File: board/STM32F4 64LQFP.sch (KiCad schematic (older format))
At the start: 15 parts, among them P2 SWD, U1 STM32F40X_LQFP64, X2 8MHz 10ppm

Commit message: - changed some more Vcc labels to +3V3 - combined all input connectors into one big connector - changed can transceiver to MAX3051 - removed HV pin from power connector -> divider now on PS board - updated components - startet layout
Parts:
- C10, C11, C12, C13, C14, C15, C16, C17, C31, C32, C35, C38: footprint CRF1:SMD-0603_c -> Capacitors_SMD:C_0805
- P2: footprint CRF1:MICRO_JST_6 -> Pin_Headers:Pin_Header_Straight_2x03
- U1: footprint CRF1:lqfp64_pad_mod -> Housings_QFP:LQFP-64_10x10mm_Pitch0.5mm
- X2: footprint CRF1:Crystal_5x3mm -> Crystals:Crystal_HC49-U_Vertical
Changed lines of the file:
@@
 F 0 "U1" H 5700 6200 60  0000 C CNN
 F 1 "STM32F40X_LQFP64" H 5750 1550 60  0000 C CNN
-F 2 "CRF1:lqfp64_pad_mod" H 5750 3900 60  0001 C CNN
+F 2 "Housings_QFP:LQFP-64_10x10mm_Pitch0.5mm" H 5750 3900 60  0001 C CNN
 F 3 "" H 5750 3900 60  0001 C CNN
 	1    5750 3900
@@
 F 0 "C17" H 7550 6450 50  0000 L CNN
 F 1 "2.2u" H 7550 6250 50  0000 L CNN
-F 2 "CRF1:SMD-0603_c" H 7500 6350 60  0001 C CNN
+F 2 "Capacitors_SMD:C_0805" H 7500 6350 60  0001 C CNN
 F 3 "" H 7500 6350 60  0001 C CNN
 	1    7500 6350
@@
 F 0 "C16" H 7550 6200 50  0000 L CNN
 F 1 "2.2u" H 7550 6000 50  0000 L CNN
-F 2 "CRF1:SMD-0603_c" H 7500 6100 60  0001 C CNN
+F 2 "Capacitors_SMD:C_0805" H 7500 6100 60  0001 C CNN
 F 3 "" H 7500 6100 60  0001 C CNN
 	1    7500 6100
@@
 $EndComp
 $Comp
-L GND-RESCUE-BLDC_4 #PWR035
+L GND-RESCUE-BLDC_4 #PWR051
 U 1 1 53F757BC
 P 8000 6050
-F 0 "#PWR035" H 8000 6050 30  0001 C CNN
+F 0 "#PWR051" H 8000 6050 30  0001 C CNN
 F 1 "GND" H 8000 5980 30  0001 C CNN
 F 2 "" H 8000 6050 60  0001 C CNN
@@
 $EndComp
 $Comp
-L GND-RESCUE-BLDC_4 #PWR037
+L GND-RESCUE-BLDC_4 #PWR052
 U 1 1 53F757C8
 P 7200 5150
-F 0 "#PWR037" H 7200 5150 30  0001 C CNN
+F 0 "#PWR052" H 7200 5150 30  0001 C CNN
 F 1 "GND" H 7200 5080 30  0001 C CNN
 F 2 "" H 7200 5150 60  0001 C CNN
@@
 F 0 "C15" H 7400 1900 50  0000 L CNN
 F 1 "15p" H 7400 1700 50  0000 L CNN
-F 2 "CRF1:SMD-0603_c" H 7350 1800 60  0001 C CNN
+F 2 "Capacitors_SMD:C_0805" H 7350 1800 60  0001 C CNN
 F 3 "" H 7350 1800 60  0001 C CNN
 	1    7350 1800
@@
 F 0 "C38" H 8150 1900 50  0000 L CNN
 F 1 "15p" H 8150 1700 50  0000 L CNN
-F 2 "CRF1:SMD-0603_c" H 8100 1800 60  0001 C CNN
+F 2 "Capacitors_SMD:C_0805" H 8100 1800 60  0001 C CNN
 F 3 "" H 8100 1800 60  0001 C CNN
 	1    8100 1800
@@
 $EndComp
 $Comp
-L GND-RESCUE-BLDC_4 #PWR039
+L GND-RESCUE-BLDC_4 #PWR053
 U 1 1 53F757E9
 P 8250 1600
-F 0 "#PWR039" H 8250 1600 30  0001 C CNN
+F 0 "#PWR053" H 8250 1600 30  0001 C CNN
 F 1 "GND" H 8250 1530 30  0001 C CNN
 F 2 "" H 8250 1600 60  0001 C CNN
@@
 $EndComp
 $Comp
-L GND-RESCUE-BLDC_4 #PWR040
+L GND-RESCUE-BLDC_4 #PWR054
 U 1 1 53F757EF
 P 7150 2550
-F 0 "#PWR040" H 7150 2550 30  0001 C CNN
+F 0 "#PWR054" H 7150 2550 30  0001 C CNN
 F 1 "GND" H 7150 2480 30  0001 C CNN
 F 2 "" H 7150 2550 60  0001 C CNN
@@
 F 0 "C31" H 7800 5550 50  0000 L CNN
 F 1 "2.2u" H 7800 5350 50  0000 L CNN
-F 2 "CRF1:SMD-0603_c" H 7750 5450 60  0001 C CNN
+F 2 "Capacitors_SMD:C_0805" H 7750 5450 60  0001 C CNN
 F 3 "" H 7750 5450 60  0001 C CNN
 	1    7750 5450
@@
 F 0 "C35" H 8050 5550 50  0000 L CNN
 F 1 "2.2u" H 8050 5350 50  0000 L CNN
-F 2 "CRF1:SMD-0603_c" H 8000 5450 60  0001 C CNN
+F 2 "Capacitors_SMD:C_0805" H 8000 5450 60  0001 C CNN
 F 3 "" H 8000 5450 60  0001 C CNN
 	1    8000 5450
@@
 NoConn ~ 4500 5450
 $Comp
-L GND-RESCUE-BLDC_4 #PWR042
+L GND-RESCUE-BLDC_4 #PWR055
 U 1 1 53F75856
 P 7950 3300
-F 0 "#PWR042" H 7950 3300 30  0001 C CNN
+F 0 "#PWR055" H 7950 3300 30  0001 C CNN
 F 1 "GND" H 7950 3230 30  0001 C CNN
 F 2 "" H 7950 3300 60  0001 C CNN
@@
 F 0 "C32" H 8000 3200 50  0000 L CNN
 F 1 "100n" H 8000 3000 50  0000 L CNN
-F 2 "CRF1:SMD-0603_c" H 7950 3100 60  0001 C CNN
+F 2 "Capacitors_SMD:C_0805" H 7950 3100 60  0001 C CNN
 F 3 "" H 7950 3100 60  0001 C CNN
 	1    7950 3100
@@
 F 0 "P2" V 10050 3150 60  0000 C CNN
 F 1 "SWD" V 10150 3150 60  0000 C CNN
-F 2 "CRF1:MICRO_JST_6" H 10100 3150 60  0001 C CNN
+F 2 "Pin_Headers:Pin_Header_Straight_2x03" H 10100 3150 60  0001 C CNN
 F 3 "" H 10100 3150 60  0001 C CNN
 	1    10100 3150
@@
 $EndComp
 $Comp
-L GND-RESCUE-BLDC_4 #PWR044
+L GND-RESCUE-BLDC_4 #PWR056
 U 1 1 53F7741D
 P 9600 3100
-F 0 "#PWR044" H 9600 3100 30  0001 C CNN
+F 0 "#PWR056" H 9600 3100 30  0001 C CNN
 F 1 "GND" H 9600 3030 30  0001 C CNN
 F 2 "" H 9600 3100 60  0001 C CNN
@@
 F 0 "C10" H 9450 1400 50  0000 L CNN
 F 1 "2.2u" H 9450 1200 50  0000 L CNN
-F 2 "CRF1:SMD-0603_c" H 9400 1300 60  0001 C CNN
+F 2 "Capacitors_SMD:C_0805" H 9400 1300 60  0001 C CNN
 F 3 "" H 9400 1300 60  0001 C CNN
 	1    9400 1300
@@
 F 0 "C11" H 9700 1400 50  0000 L CNN
 F 1 "2.2u" H 9700 1200 50  0000 L CNN
-F 2 "CRF1:SMD-0603_c" H 9650 1300 60  0001 C CNN
+F 2 "Capacitors_SMD:C_0805" H 9650 1300 60  0001 C CNN
 F 3 "" H 9650 1300 60  0001 C CNN
 	1    9650 1300
@@
 F 0 "C14" H 10450 1400 50  0000 L CNN
 F 1 "2.2u" H 10450 1200 50  0000 L CNN
-F 2 "CRF1:SMD-0603_c" H 10400 1300 60  0001 C CNN
+F 2 "Capacitors_SMD:C_0805" H 10400 1300 60  0001 C CNN
 F 3 "" H 10400 1300 60  0001 C CNN
 	1    10400 1300
@@
 $EndComp
 $Comp
-L GND-RESCUE-BLDC_4 #PWR045
+L GND-RESCUE-BLDC_4 #PWR057
 U 1 1 53F7743B
 P 9100 1650
-F 0 "#PWR045" H 9100 1650 30  0001 C CNN
+F 0 "#PWR057" H 9100 1650 30  0001 C CNN
 F 1 "GND" H 9100 1580 30  0001 C CNN
 F 2 "" H 9100 1650 60  0001 C CNN
@@
 F 0 "C12" H 9950 1400 50  0000 L CNN
 F 1 "2.2u" H 9950 1200 50  0000 L CNN
-F 2 "CRF1:SMD-0603_c" H 9900 1300 60  0001 C CNN
+F 2 "Capacitors_SMD:C_0805" H 9900 1300 60  0001 C CNN
 F 3 "" H 9900 1300 60  0001 C CNN
 	1    9900 1300
@@
 F 0 "C13" H 10200 1400 50  0000 L CNN
 F 1 "2.2u" H 10200 1200 50  0000 L CNN
-F 2 "CRF1:SMD-0603_c" H 10150 1300 60  0001 C CNN
+F 2 "Capacitors_SMD:C_0805" H 10150 1300 60  0001 C CNN
 F 3 "" H 10150 1300 60  0001 C CNN
 	1    10150 1300
@@
 00 00 00 50 18 A4 4F 00 00 00 40 61 90 3E 01 00 00 00 85 41 FA 04 00 00 00 14 06 E9 13 00 00 00
 50 18 A4 4F 00 00 00 40 61 90 3E 01 00 00 00 85 41 FA 04 00 00 00 14 F6 FF 00 CF 05 3E 3D 48 21
-47 45 00 00 00 00 49 45 4E 44 AE 42 60 82 45
+47 45 00 00 00 00 49 45 4E 44 AE 42 60 82 03
 EndData
 $EndBitmap
@@
 9D 20 C6 37 81 40 20 10 08 04 02 81 D0 4E 10 E3 9B 40 20 10 08 04 02 81 40 68 27 88 F1 4D 20 10
 08 04 02 81 40 20 B4 13 C4 F8 26 10 08 04 02 81 40 20 10 DA 89 FF 07 6E 76 4C 5E B7 9B F3 6C 00
-00 00 00 49 45 4E 44 AE 42 60 82 4C
+00 00 00 49 45 4E 44 AE 42 60 82 17
 EndData
 $EndBitmap
@@
 F 0 "X2" H 7750 2140 30  0000 C CNN
 F 1 "8MHz 10ppm" H 7800 1950 30  0000 L CNN
-F 2 "CRF1:Crystal_5x3mm" H 7750 2050 60  0001 C CNN
+F 2 "Crystals:Crystal_HC49-U_Vertical" H 7750 2050 60  0001 C CNN
 F 3 "" H 7750 2050 60  0000 C CNN
 F 4 "ABM3B-8.0-10-1UT" H 7750 2050 60  0001 C CNN "mfg#"
@@
 $EndComp
 $Comp
-L GND-RESCUE-BLDC_4 #PWR047
+L GND-RESCUE-BLDC_4 #PWR058
 U 1 1 54097D19
 P 7750 2150
-F 0 "#PWR047" H 7750 2150 30  0001 C CNN
+F 0 "#PWR058" H 7750 2150 30  0001 C CNN
 F 1 "GND" H 7750 2080 30  0001 C CNN
 F 2 "" H 7750 2150 60  0001 C CNN
@@
 TX_SDA_NSS
 $Comp
-L +3V3 #PWR?
+L +3V3 #PWR059
 U 1 1 57529FFB
 P 7200 4200
-F 0 "#PWR?" H 7200 4050 50  0001 C CNN
+F 0 "#PWR059" H 7200 4050 50  0001 C CNN
 F 1 "+3V3" H 7200 4340 50  0000 C CNN
 F 2 "" H 7200 4200 50  0000 C CNN
@@
 $EndComp
 $Comp
-L +3V3 #PWR?
+L +3V3 #PWR060
 U 1 1 5752A2EE
 P 7400 5100
-F 0 "#PWR?" H 7400 4950 50  0001 C CNN
+F 0 "#PWR060" H 7400 4950 50  0001 C CNN
 F 1 "+3V3" H 7400 5240 50  0000 C CNN
 F 2 "" H 7400 5100 50  0000 C CNN
@@
 $EndComp
 $Comp
-L +3V3 #PWR?
+L +3V3 #PWR061
 U 1 1 5752A326
 P 7200 5350
-F 0 "#PWR?" H 7200 5200 50  0001 C CNN
+F 0 "#PWR061" H 7200 5200 50  0001 C CNN
 F 1 "+3V3" H 7050 5400 50  0000 C CNN
 F 2 "" H 7200 5350 50  0000 C CNN
@@
 $EndComp
 $Comp
-L +3V3 #PWR?
+L +3V3 #PWR062
 U 1 1 5752A907
 P 9750 2900
-F 0 "#PWR?" H 9750 2750 50  0001 C CNN
+F 0 "#PWR062" H 9750 2750 50  0001 C CNN
 F 1 "+3V3" V 9750 3150 50  0000 C CNN
 F 2 "" H 9750 2900 50  0000 C CNN
@@
 $EndComp
 $Comp
-L +3V3 #PWR?
+L +3V3 #PWR063
 U 1 1 5752A9C6
 P 9100 950
-F 0 "#PWR?" H 9100 800 50  0001 C CNN
+F 0 "#PWR063" H 9100 800 50  0001 C CNN
 F 1 "+3V3" H 9100 1090 50  0000 C CNN
 F 2 "" H 9100 950 50  0000 C CNN

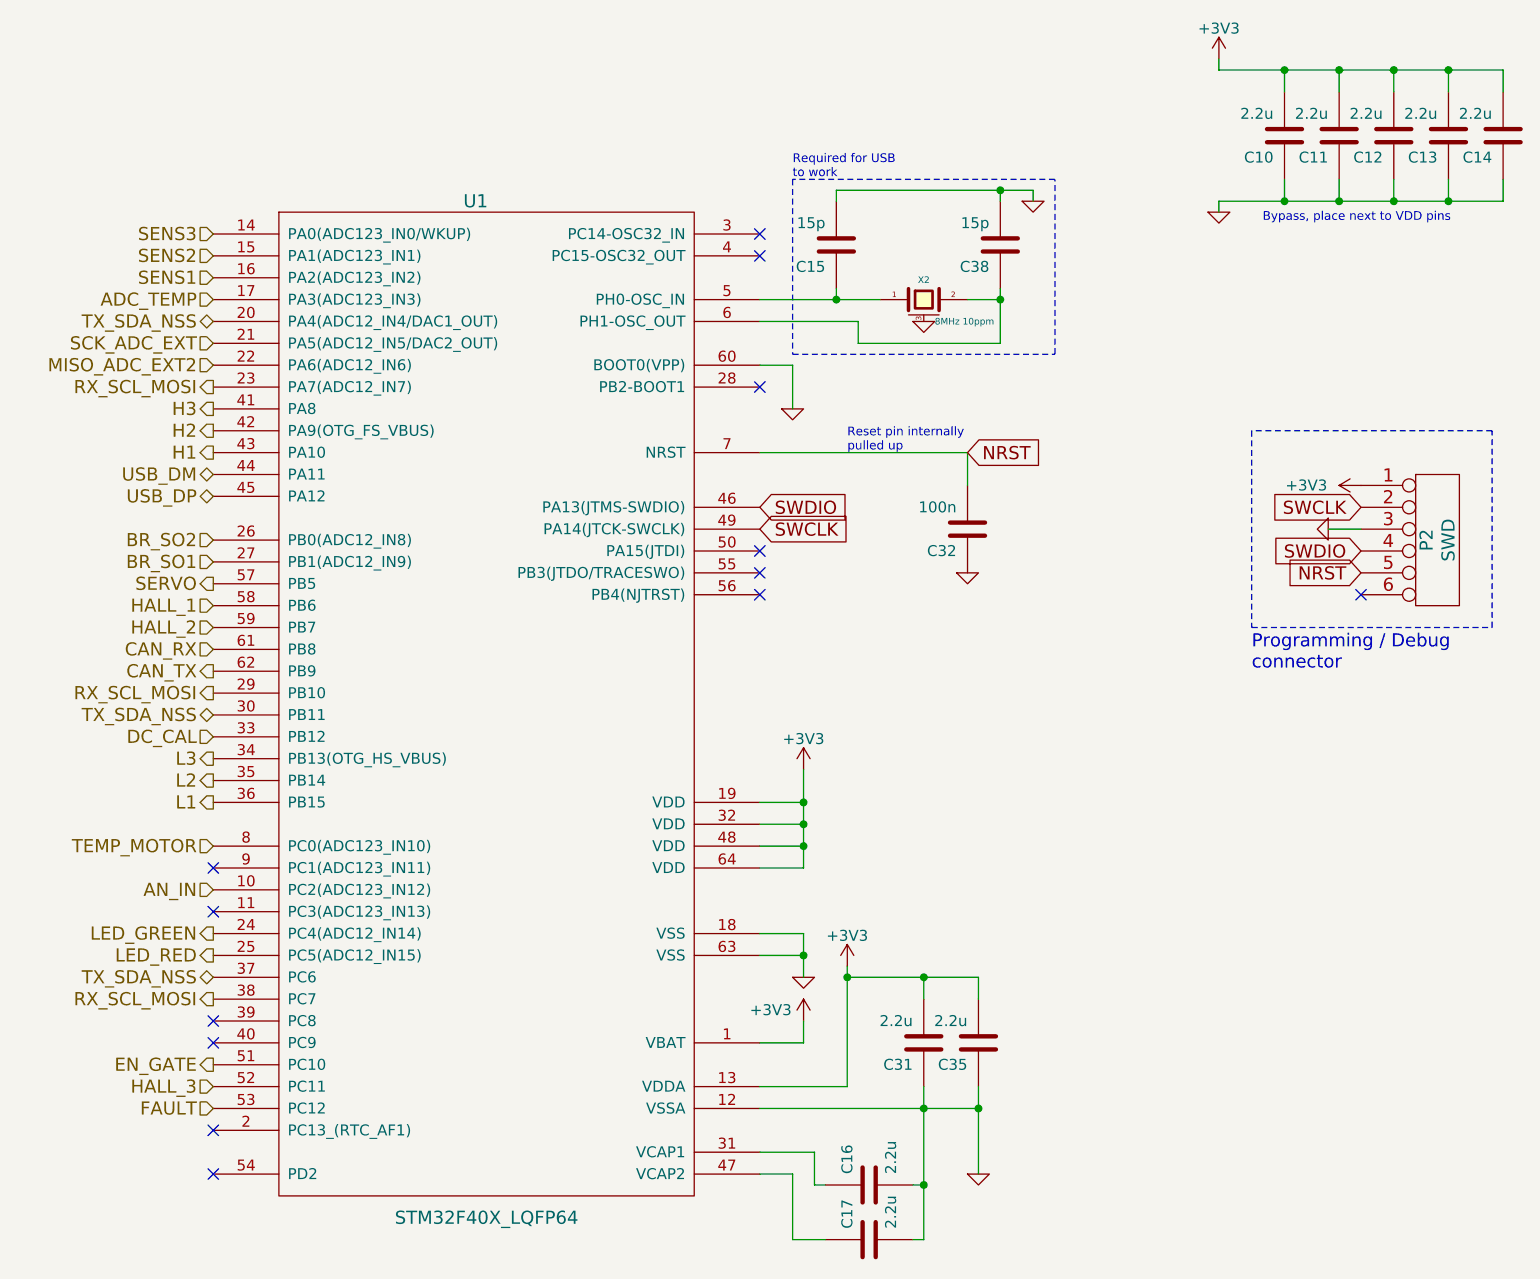
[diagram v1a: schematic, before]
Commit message: - preliminary layout for CPU board ready
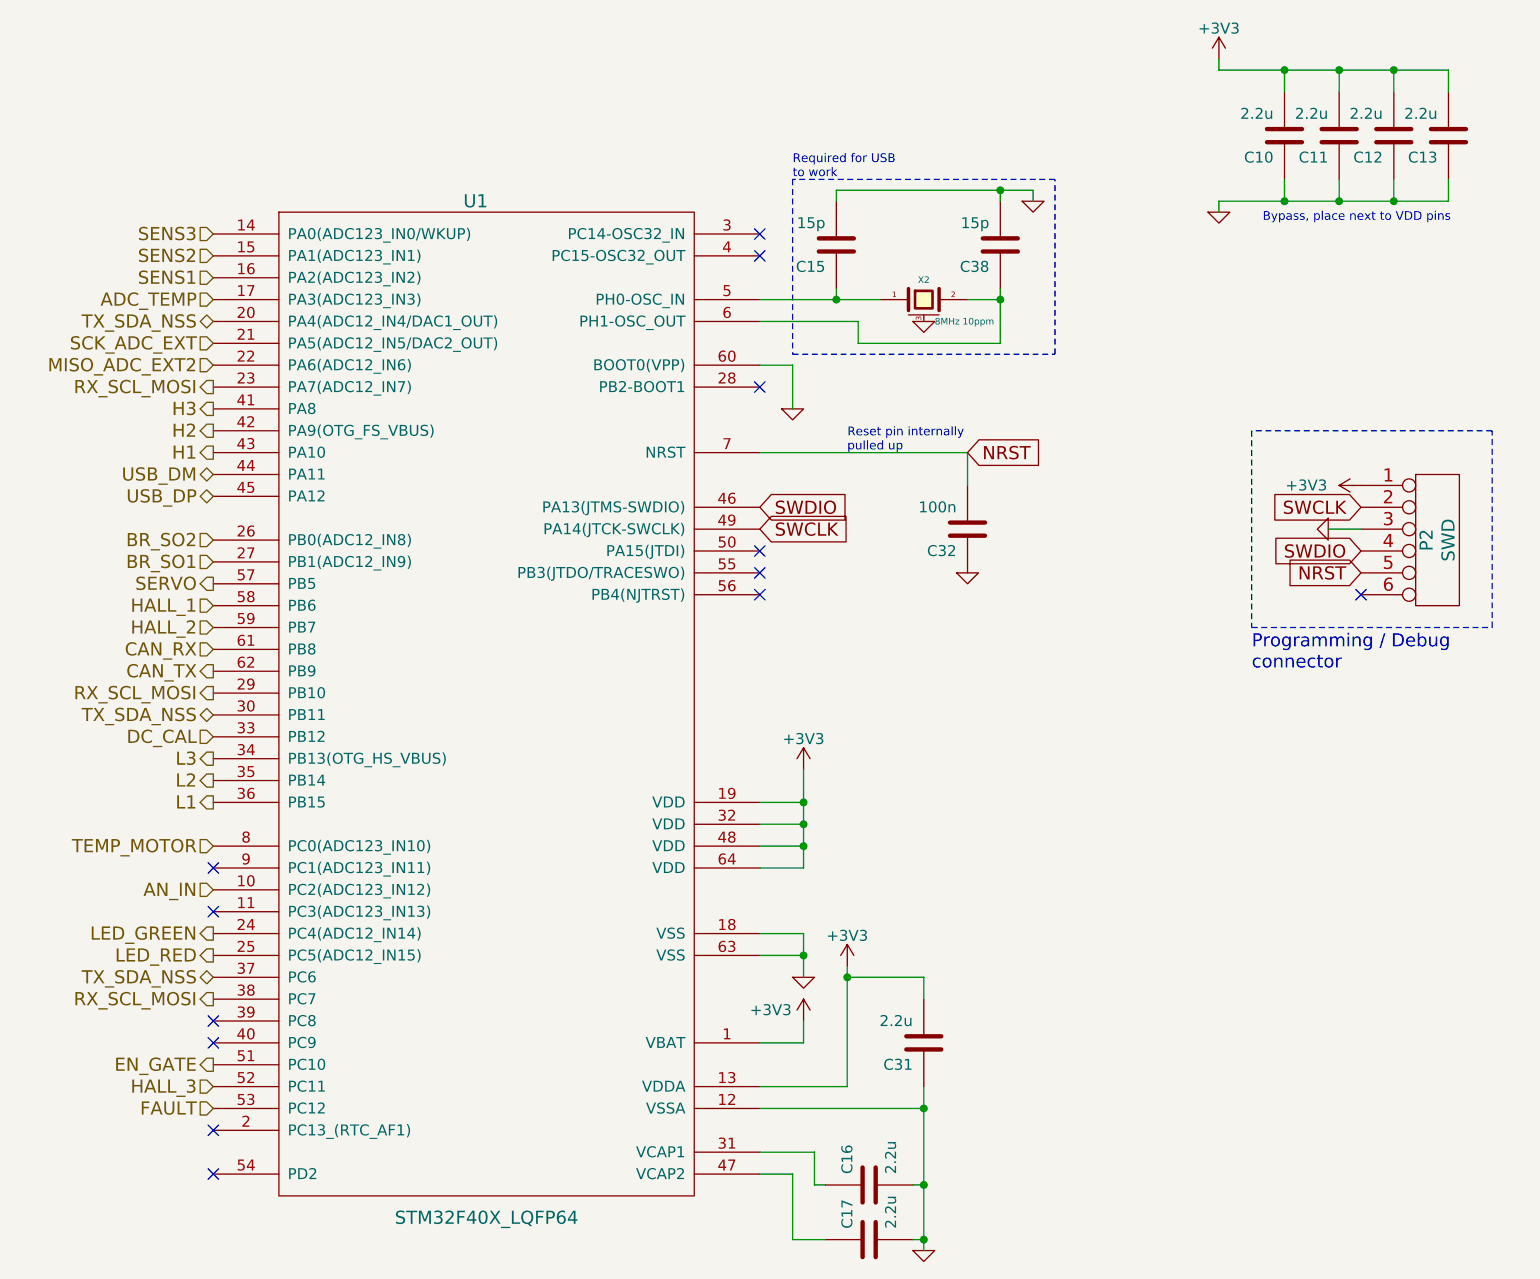
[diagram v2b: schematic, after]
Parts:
- removed C14, C35: 2.2u, Capacitors_SMD:C_0805, symbol C-RESCUE-BLDC_4
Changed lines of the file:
@@
 $EndComp
 $Comp
-L GND-RESCUE-BLDC_4 #PWR051
+L GND-RESCUE-BLDC_4 #PWR058
 U 1 1 53F757BC
-P 8000 6050
-F 0 "#PWR051" H 8000 6050 30  0001 C CNN
-F 1 "GND" H 8000 5980 30  0001 C CNN
-F 2 "" H 8000 6050 60  0001 C CNN
-F 3 "" H 8000 6050 60  0001 C CNN
-	1    8000 6050
+P 7750 6400
+F 0 "#PWR058" H 7750 6400 30  0001 C CNN
+F 1 "GND" H 7750 6330 30  0001 C CNN
+F 2 "" H 7750 6400 60  0001 C CNN
+F 3 "" H 7750 6400 60  0001 C CNN
+	1    7750 6400
 	1    0    0    -1
 $EndComp
 $Comp
-L GND-RESCUE-BLDC_4 #PWR052
+L GND-RESCUE-BLDC_4 #PWR059
 U 1 1 53F757C8
 P 7200 5150
-F 0 "#PWR052" H 7200 5150 30  0001 C CNN
+F 0 "#PWR059" H 7200 5150 30  0001 C CNN
 F 1 "GND" H 7200 5080 30  0001 C CNN
 F 2 "" H 7200 5150 60  0001 C CNN
@@
 $EndComp
 $Comp
-L GND-RESCUE-BLDC_4 #PWR053
+L GND-RESCUE-BLDC_4 #PWR060
 U 1 1 53F757E9
 P 8250 1600
-F 0 "#PWR053" H 8250 1600 30  0001 C CNN
+F 0 "#PWR060" H 8250 1600 30  0001 C CNN
 F 1 "GND" H 8250 1530 30  0001 C CNN
 F 2 "" H 8250 1600 60  0001 C CNN
@@
 $EndComp
 $Comp
-L GND-RESCUE-BLDC_4 #PWR054
+L GND-RESCUE-BLDC_4 #PWR061
 U 1 1 53F757EF
 P 7150 2550
-F 0 "#PWR054" H 7150 2550 30  0001 C CNN
+F 0 "#PWR061" H 7150 2550 30  0001 C CNN
 F 1 "GND" H 7150 2480 30  0001 C CNN
 F 2 "" H 7150 2550 60  0001 C CNN
@@
 	-1   0    0    1
 $EndComp
-$Comp
-L C-RESCUE-BLDC_4 C35
-U 1 1 53F757FF
-P 8000 5450
-F 0 "C35" H 8050 5550 50  0000 L CNN
-F 1 "2.2u" H 8050 5350 50  0000 L CNN
-F 2 "Capacitors_SMD:C_0805" H 8000 5450 60  0001 C CNN
-F 3 "" H 8000 5450 60  0001 C CNN
-	1    8000 5450
-	-1   0    0    1
-$EndComp
 NoConn ~ 7000 2450
 NoConn ~ 7000 3200
@@
 NoConn ~ 4500 5450
 $Comp
-L GND-RESCUE-BLDC_4 #PWR055
+L GND-RESCUE-BLDC_4 #PWR062
 U 1 1 53F75856
 P 7950 3300
-F 0 "#PWR055" H 7950 3300 30  0001 C CNN
+F 0 "#PWR062" H 7950 3300 30  0001 C CNN
 F 1 "GND" H 7950 3230 30  0001 C CNN
 F 2 "" H 7950 3300 60  0001 C CNN
@@
 Wire Wire Line
 	7000 5450 7200 5450
-Connection ~ 8000 5750
-Connection ~ 7750 5150
-Wire Wire Line
-	8000 5150 8000 5250
 Connection ~ 7400 5150
 Wire Wire Line
-	7400 5150 8000 5150
-Wire Wire Line
 	7750 5250 7750 5150
 Wire Wire Line
@@
 Connection ~ 7750 5750
 Wire Wire Line
-	8000 5650 8000 6050
-Wire Wire Line
 	7150 6350 7300 6350
 Wire Wire Line
@@
 Connection ~ 7750 6100
 Wire Wire Line
-	7000 5750 8000 5750
-Wire Wire Line
-	7750 5650 7750 6350
+	7750 5650 7750 6400
 Wire Wire Line
 	7750 6100 7700 6100
@@
 $EndComp
 $Comp
-L GND-RESCUE-BLDC_4 #PWR056
+L GND-RESCUE-BLDC_4 #PWR063
 U 1 1 53F7741D
 P 9600 3100
-F 0 "#PWR056" H 9600 3100 30  0001 C CNN
+F 0 "#PWR063" H 9600 3100 30  0001 C CNN
 F 1 "GND" H 9600 3030 30  0001 C CNN
 F 2 "" H 9600 3100 60  0001 C CNN
@@
 $EndComp
 $Comp
-L C-RESCUE-BLDC_4 C14
-U 1 1 53F77434
-P 10400 1300
-F 0 "C14" H 10450 1400 50  0000 L CNN
-F 1 "2.2u" H 10450 1200 50  0000 L CNN
-F 2 "Capacitors_SMD:C_0805" H 10400 1300 60  0001 C CNN
-F 3 "" H 10400 1300 60  0001 C CNN
-	1    10400 1300
-	-1   0    0    1
-$EndComp
-$Comp
-L GND-RESCUE-BLDC_4 #PWR057
+L GND-RESCUE-BLDC_4 #PWR064
 U 1 1 53F7743B
 P 9100 1650
-F 0 "#PWR057" H 9100 1650 30  0001 C CNN
+F 0 "#PWR064" H 9100 1650 30  0001 C CNN
 F 1 "GND" H 9100 1580 30  0001 C CNN
 F 2 "" H 9100 1650 60  0001 C CNN
@@
 	-1   0    0    1
 $EndComp
-Connection ~ 10150 1600
 Wire Wire Line
 	10150 1600 10150 1500
@@
 Wire Wire Line
 	9900 1000 9900 1100
-Connection ~ 10150 1000
 Wire Wire Line
 	10150 1000 10150 1100
 Wire Wire Line
-	10400 1000 10400 1100
-Wire Wire Line
-	9100 1000 10400 1000
-Wire Wire Line
 	9100 950  9100 1000
 Wire Wire Line
-	10400 1600 10400 1500
-Wire Wire Line
-	9100 1600 10400 1600
-Wire Wire Line
 	9100 1650 9100 1600
 Wire Wire Line
@@
 00 00 00 50 18 A4 4F 00 00 00 40 61 90 3E 01 00 00 00 85 41 FA 04 00 00 00 14 06 E9 13 00 00 00
 50 18 A4 4F 00 00 00 40 61 90 3E 01 00 00 00 85 41 FA 04 00 00 00 14 F6 FF 00 CF 05 3E 3D 48 21
-47 45 00 00 00 00 49 45 4E 44 AE 42 60 82 03
+47 45 00 00 00 00 49 45 4E 44 AE 42 60 82 1B
 EndData
 $EndBitmap
@@
 9D 20 C6 37 81 40 20 10 08 04 02 81 D0 4E 10 E3 9B 40 20 10 08 04 02 81 40 68 27 88 F1 4D 20 10
 08 04 02 81 40 20 B4 13 C4 F8 26 10 08 04 02 81 40 20 10 DA 89 FF 07 6E 76 4C 5E B7 9B F3 6C 00
-00 00 00 49 45 4E 44 AE 42 60 82 17
+00 00 00 49 45 4E 44 AE 42 60 82 80
 EndData
 $EndBitmap
@@
 $EndComp
 $Comp
-L GND-RESCUE-BLDC_4 #PWR058
+L GND-RESCUE-BLDC_4 #PWR065
 U 1 1 54097D19
 P 7750 2150
-F 0 "#PWR058" H 7750 2150 30  0001 C CNN
+F 0 "#PWR065" H 7750 2150 30  0001 C CNN
 F 1 "GND" H 7750 2080 30  0001 C CNN
 F 2 "" H 7750 2150 60  0001 C CNN
@@
 TX_SDA_NSS
 $Comp
-L +3V3 #PWR059
+L +3V3 #PWR066
 U 1 1 57529FFB
 P 7200 4200
-F 0 "#PWR059" H 7200 4050 50  0001 C CNN
+F 0 "#PWR066" H 7200 4050 50  0001 C CNN
 F 1 "+3V3" H 7200 4340 50  0000 C CNN
 F 2 "" H 7200 4200 50  0000 C CNN
@@
 $EndComp
 $Comp
-L +3V3 #PWR060
+L +3V3 #PWR067
 U 1 1 5752A2EE
 P 7400 5100
-F 0 "#PWR060" H 7400 4950 50  0001 C CNN
+F 0 "#PWR067" H 7400 4950 50  0001 C CNN
 F 1 "+3V3" H 7400 5240 50  0000 C CNN
 F 2 "" H 7400 5100 50  0000 C CNN
@@
 $EndComp
 $Comp
-L +3V3 #PWR061
+L +3V3 #PWR068
 U 1 1 5752A326
 P 7200 5350
-F 0 "#PWR061" H 7200 5200 50  0001 C CNN
+F 0 "#PWR068" H 7200 5200 50  0001 C CNN
 F 1 "+3V3" H 7050 5400 50  0000 C CNN
 F 2 "" H 7200 5350 50  0000 C CNN
@@
 $EndComp
 $Comp
-L +3V3 #PWR062
+L +3V3 #PWR069
 U 1 1 5752A907
 P 9750 2900
-F 0 "#PWR062" H 9750 2750 50  0001 C CNN
+F 0 "#PWR069" H 9750 2750 50  0001 C CNN
 F 1 "+3V3" V 9750 3150 50  0000 C CNN
 F 2 "" H 9750 2900 50  0000 C CNN
@@
 $EndComp
 $Comp
-L +3V3 #PWR063
+L +3V3 #PWR070
 U 1 1 5752A9C6
 P 9100 950
-F 0 "#PWR063" H 9100 800 50  0001 C CNN
+F 0 "#PWR070" H 9100 800 50  0001 C CNN
 F 1 "+3V3" H 9100 1090 50  0000 C CNN
 F 2 "" H 9100 950 50  0000 C CNN
@@
 	1    0    0    -1
 $EndComp
+Wire Wire Line
+	7000 5750 7750 5750
+Wire Wire Line
+	7750 5150 7400 5150
+Connection ~ 7750 6350
+Wire Wire Line
+	9100 1000 10150 1000
+Wire Wire Line
+	9100 1600 10150 1600
 $EndSCHEMATC
